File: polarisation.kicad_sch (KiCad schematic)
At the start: 24 parts, among them J1 HV400_IN, Q3 BSS127I, Q4 MMBT2222, Q5 BSS127I, U10 ISO7710, U11 AMC0311R

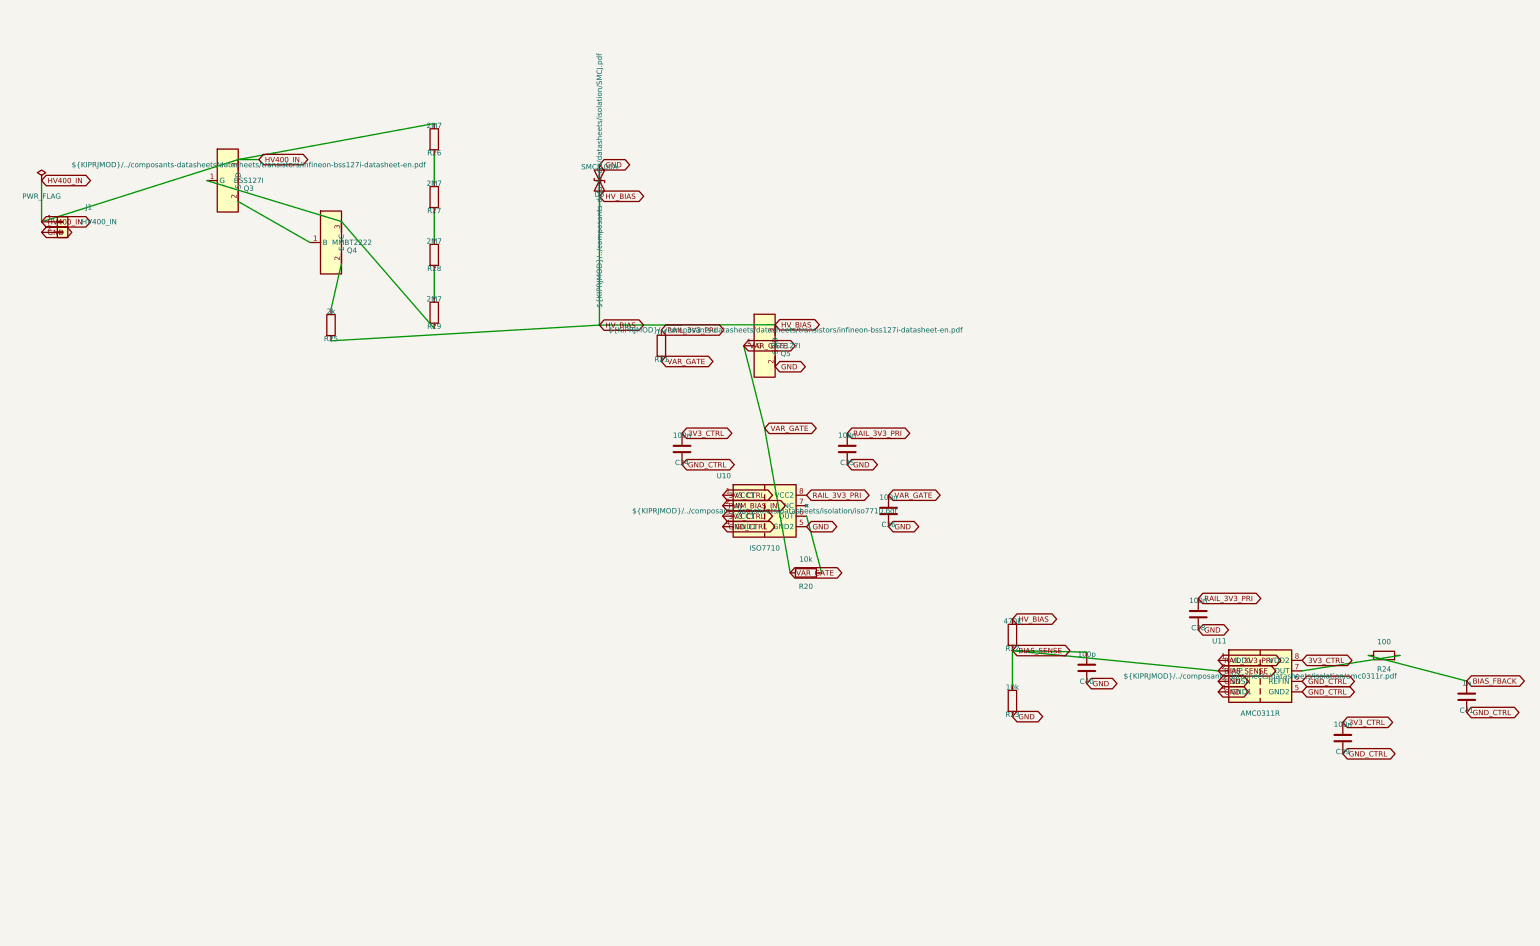
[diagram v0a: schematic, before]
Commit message: Retours temperature/courant primaire isoles, isolation C2000 reelle, feuille Polarisation finalisee (80V, R26 corrige par simulation)
- U8 (AMC0311R) : retour temperature primaire (thermistance NTC) isole
- U9 (AMC0302R) : retour courant primaire (shunt R19) isole
- Migration GND_CTRL/3V3_CTRL : le C2000 externe recoit ses propres nets
  d'alimentation/masse isoles (U3/U4/U5/U7/U8/U9), connecteurs CpuOut/CpuIn
  agrandis a 16 broches
- Feuille polarisation.kicad_sch reprise en etiquettes globales uniquement
  (plus de fils explicites) et alignee sur la grille 1.27mm
- Source de courant Q3/Q4/R25/R26 simplifiee a un rail fixe 80V (HV80_IN,
  ex-400V) ; R26 corrige de 2M7 a 75k apres simulation SPICE (ngspice,
  modeles reels Diodes Inc.) qui a revele que le montage se comporte
  comme une resistance plutot qu'une source plate - voir 00-intention-
  conception.md §15bis
- Nouveau script bom_family_report.py (remplace BOMconverter.py) :
  nomenclature groupee par famille, sans dependance externe, lit soit le
  netlist XML legacy d'Eeschema soit un CSV kicad-cli
- README.md : image du schema integree
- Mise a jour 00-intention-conception.md (§13-15bis)

Co-Authored-By: Claude Sonnet 5 <noreply@anthropic.com>
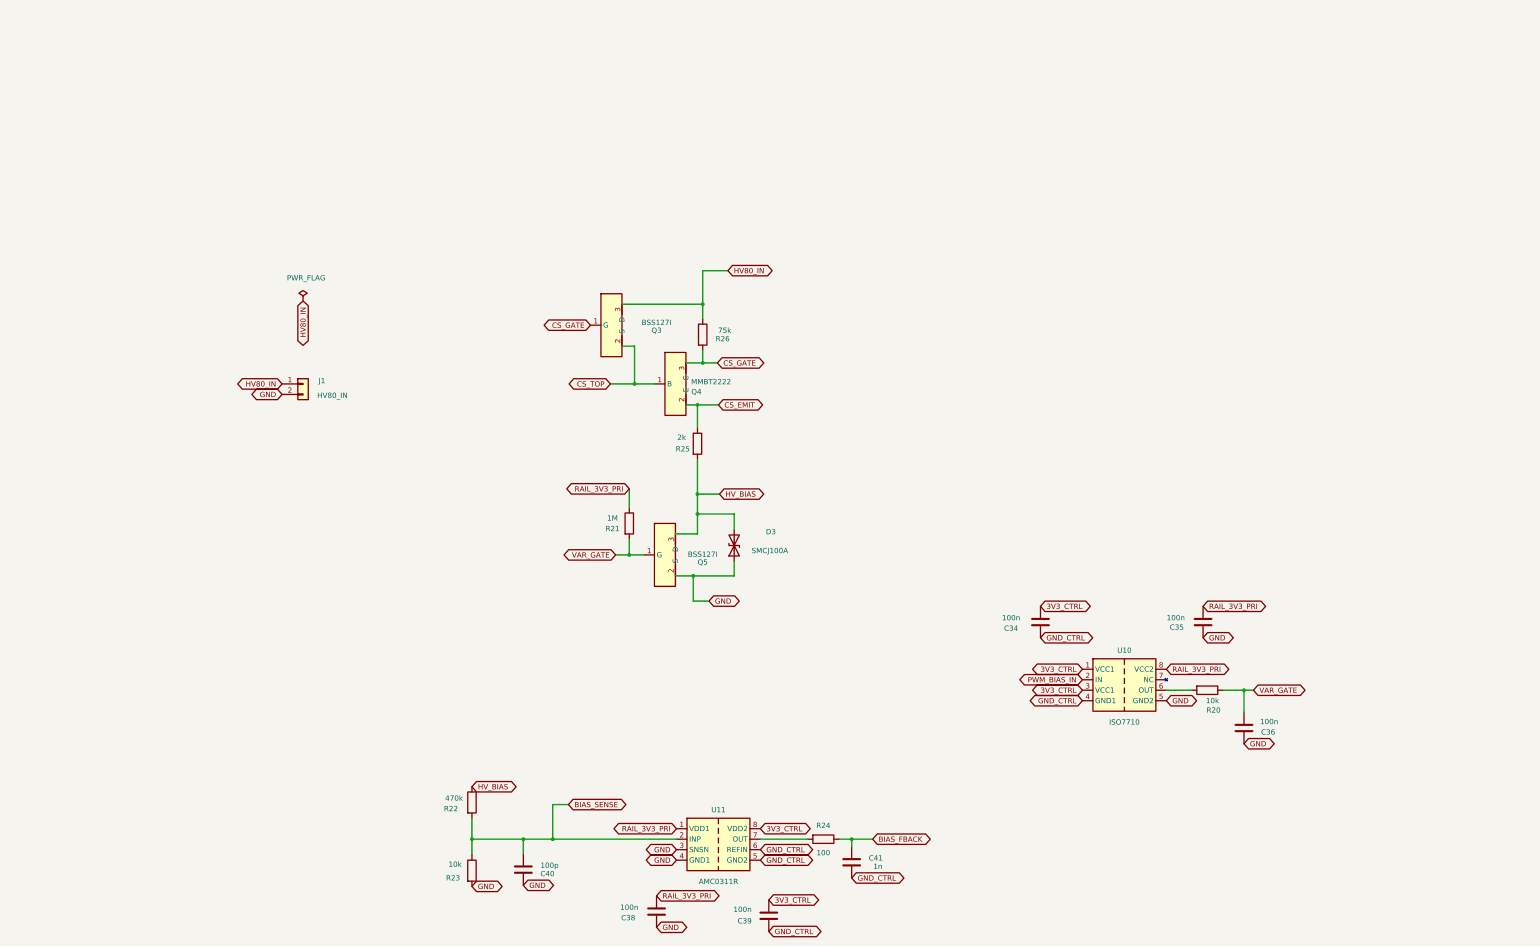
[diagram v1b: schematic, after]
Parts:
- removed R27, R28, R29: 2M7, Resistor_SMD:R_0805_2012Metric, symbol Device:R
- J1: value HV400_IN -> HV80_IN
- R26: value 2M7 -> 75k
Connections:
- net CS_GATE: now reaches R26.2
- net CS_GATE: now also Q3.1 (G), Q4.3 (C)
- net CS_TOP: now reaches Q3.2 (S), Q4.1 (B)
- net CS_EMIT: now reaches Q4.2 (E), R25.1
- net HV400_IN renamed HV80_IN

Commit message: Remplace CpuOut1/CpuIn1 par un connecteur J2 unique, aligné pin-a-pin sur J21 du shield
KICAD-C2000-powershield a desormais un connecteur IDC 2x10 dedie
(J21/NAPPE_FILAMENT_HT, decision #26) a la place du partage de nappes
generiques. J2 reprend exactement ce brochage ; 7 nets renommes pour
matcher le vocabulaire du shield (PWM_ht, PWM_EN, PWM_bias, Vht,
Temp_ht, I_Shunt_ht, V_bias, 3V3_ISO). GND_CTRL volontairement non
renomme en GND : KICAD-HT a deja un net GND distinct (masse primaire
non isolee), renommer aurait fusionne les deux domaines par coincidence
de nom. Vht_EN et I_Shunt_ht_comp poses mais non cables en interne
(reserve / futur trip rapide), par decision explicite.

ERC hierarchie complete : 0 erreur, 219 avertissements de la meme
famille qu'avant ce changement.

Co-Authored-By: Claude Sonnet 5 <noreply@anthropic.com>
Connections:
- net 3V3_CTRL renamed 3V3_ISO
- net BIAS_FBACK renamed V_bias
- net PWM_BIAS_IN renamed PWM_bias
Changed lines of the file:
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@@
 		)
 	)
-	(global_label "BIAS_FBACK"
+	(global_label "V_bias"
 		(shape bidirectional)
 		(at 216.154 189.484 0)
@@
 		)
 	)
-	(global_label "3V3_CTRL"
+	(global_label "3V3_ISO"
 		(shape bidirectional)
 		(at 191.008 204.216 0)
@@
 		)
 	)
-	(global_label "3V3_CTRL"
+	(global_label "3V3_ISO"
 		(shape bidirectional)
 		(at 266.954 153.416 180)
@@
 		)
 	)
-	(global_label "3V3_CTRL"
+	(global_label "3V3_ISO"
 		(shape bidirectional)
 		(at 188.976 186.944 0)
@@
 		)
 	)
-	(global_label "PWM_BIAS_IN"
+	(global_label "PWM_bias"
 		(shape bidirectional)
 		(at 266.954 150.876 180)
@@
 		)
 	)
-	(global_label "3V3_CTRL"
+	(global_label "3V3_ISO"
 		(shape bidirectional)
 		(at 266.954 148.336 180)
@@
 		)
 	)
-	(global_label "3V3_CTRL"
+	(global_label "3V3_ISO"
 		(shape bidirectional)
 		(at 256.794 133.096 0)
